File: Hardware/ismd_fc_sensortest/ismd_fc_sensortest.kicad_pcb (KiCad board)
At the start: 2 copper layers, 28 parts, among them U1 TEENSY_4.1

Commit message: sensortest work
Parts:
- removed C19, C20, C21: 100nF, Capacitor_SMD:C_0402_1005Metric
- added C1: 100nF, Capacitor_SMD:C_0201_0603Metric, F.Cu at (42.5, 25.0)
- added C10: 0.1uF, Capacitor_SMD:C_0201_0603Metric, F.Cu at (36.3, 46.0)
- added C2: 100nF, Capacitor_SMD:C_0201_0603Metric, F.Cu at (44.4, 26.1)
- C11: value 0.1uF -> 2.2uF; footprint Capacitor_SMD:C_0402_1005Metric -> Capacitor_SMD:C_0201_0603Metric
- C12: value 2.2uF -> 10nF; footprint Capacitor_SMD:C_0402_1005Metric -> Capacitor_SMD:C_0201_0603Metric
- C13: value 10nF -> 100nF; footprint Capacitor_SMD:C_0402_1005Metric -> Capacitor_SMD:C_0201_0603Metric
- C14, C15, C16, C17, C18, C3, C4, C5, C6, C7, C8, C9: footprint Capacitor_SMD:C_0402_1005Metric -> Capacitor_SMD:C_0201_0603Metric
- I4: value ISM330DLCTR -> ISM330DLC
- moved I2 94.5 mm to (24.5, 26.7)
- moved I3 91.2 mm to (24.7, 35.5)
- moved I4 88.2 mm to (24.6, 44.5)
- moved B4 81.0 mm to (33.5, 26.3), turned to 90 degrees
- moved B5 75.8 mm to (33.6, 35.5)
- moved I1 72.3 mm to (33.7, 44.5)
- moved B1 65.3 mm to (42.4, 26.6)
- moved B2 62.5 mm to (42.5, 35.7)
- moved B3 58.5 mm to (42.8, 44.5)
- moved C5 31.7 mm to (42.9, 46.2)
- moved C6 26.7 mm to (42.5, 42.8), turned to 180 degrees
- moved C11 23.0 mm to (36.3, 45.2), turned to 180 degrees
- moved C12 21.7 mm to (33.5, 46.5)
- moved C16 20.9 mm to (24.5, 37.5)
- moved C8 20.5 mm to (33.4, 33.8), turned to 180 degrees
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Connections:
- C12 pad 1: GND -> +3V3
- C12 pad 2: +3V3 -> GND
- C16 pad 1: GND -> +3V3
- C16 pad 2: +3V3 -> GND
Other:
- board outline added: 102.7 x 40 mm

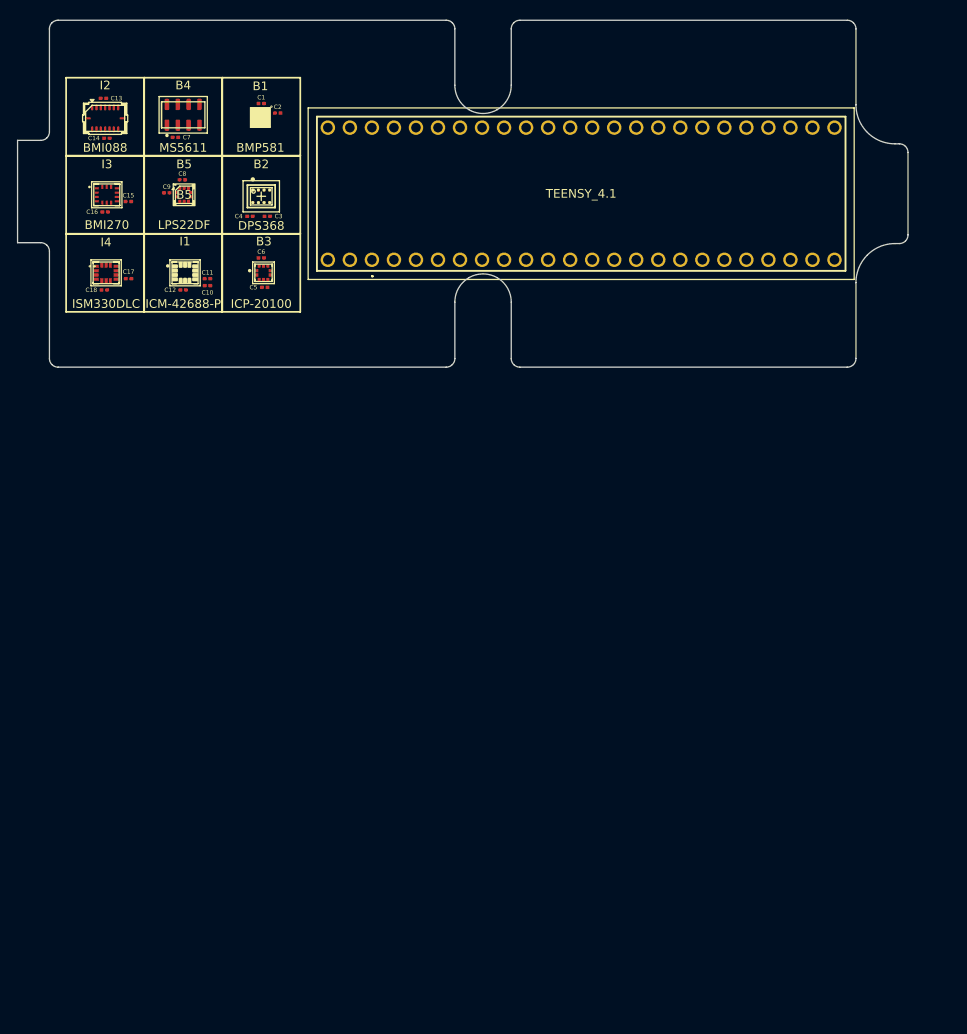
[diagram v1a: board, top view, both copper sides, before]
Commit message: added mounting holes to sensortest
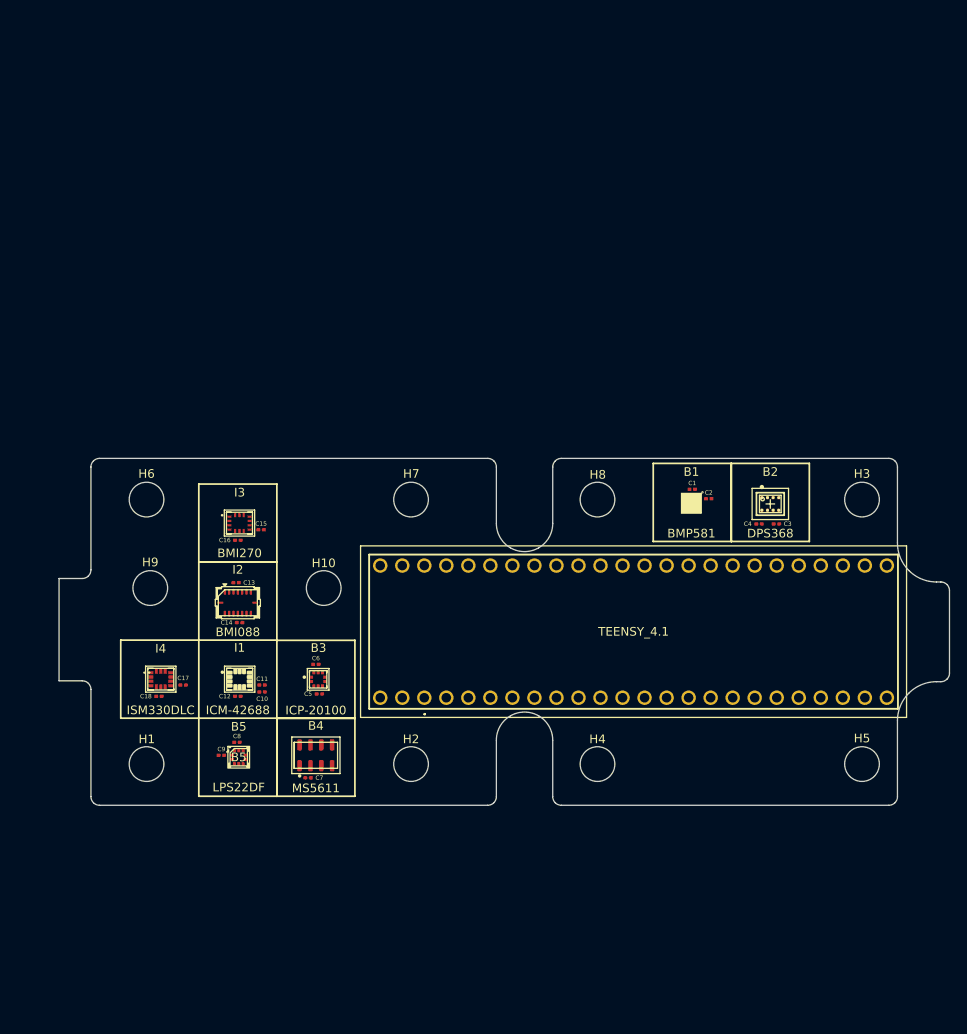
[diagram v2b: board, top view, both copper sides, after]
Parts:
- added H1: MountingHole, MountingHole:MountingHole_4mm, F.Cu at (29.3, 101.2)
- added H10: MountingHole, MountingHole:MountingHole_4mm, F.Cu at (49.7, 80.9)
- added H2: MountingHole, MountingHole:MountingHole_4mm, F.Cu at (59.8, 101.2)
- added H3: MountingHole, MountingHole:MountingHole_4mm, F.Cu at (111.8, 70.7)
- added H4: MountingHole, MountingHole:MountingHole_4mm, F.Cu at (81.3, 101.2)
- added H5: MountingHole, MountingHole:MountingHole_4mm, F.Cu at (111.8, 101.2)
- added H6: MountingHole, MountingHole:MountingHole_4mm, F.Cu at (29.3, 70.7)
- added H7: MountingHole, MountingHole:MountingHole_4mm, F.Cu at (59.8, 70.7)
- added H8: MountingHole, MountingHole:MountingHole_4mm, F.Cu at (81.3, 70.7)
- added H9: MountingHole, MountingHole:MountingHole_4mm, F.Cu at (29.7, 80.9)
- I1: value ICM-42688-P -> ICM-42688
- moved C7 75.4 mm to (47.9, 102.8)
- moved B4 75.4 mm to (48.8, 100.2)
- moved B2 68.6 mm to (101.2, 71.2)
- moved C3 68.6 mm to (101.9, 73.5)
- moved C4 68.6 mm to (99.9, 73.5)
- moved B1 66.7 mm to (92.1, 71.1)
- moved C1 66.7 mm to (92.2, 69.5)
- moved C2 66.7 mm to (94.1, 70.6)
- moved B5 65.2 mm to (39.9, 100.4)
- moved C8 65.2 mm to (39.7, 98.7)
- moved C9 65.2 mm to (37.9, 100.2)
- moved C14 57.9 mm to (40.0, 84.9)
- moved C13 57.9 mm to (39.6, 80.3)
- moved I2 57.9 mm to (39.8, 82.6)
- moved U1 50.9 mm to (61.3, 93.5)
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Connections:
- U1 pad 1: /CS_B6 -> unconnected-(U1-TX1-Pad1)
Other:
- outline, holes or cut-outs redrawn

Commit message: remove mpu holes in sensortest
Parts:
- removed H10, H9: MountingHole, MountingHole:MountingHole_4mm
- U1: value TEENSY_4.1 -> TEENSY 4.1
- moved C17 20.5 mm to (51.5, 82.1)
- moved I4 20.5 mm to (48.9, 81.4)
- moved C18 20.5 mm to (48.7, 83.4)
- moved B3 0.96 mm to (49.0, 90.4)
- moved B5 0.96 mm to (39.9, 99.4)
- moved C5 0.96 mm to (49.2, 92.1)
- moved C8 0.96 mm to (39.7, 97.7)
- moved I1 0.96 mm to (40.0, 90.4)
- moved B4 0.96 mm to (48.8, 99.2)
- moved C10 0.96 mm to (42.6, 91.9)
- moved C11 0.96 mm to (42.6, 91.1)
- moved C12 0.96 mm to (39.8, 92.4)
- moved C13 0.96 mm to (39.6, 79.3)
- moved C14 0.96 mm to (40.0, 83.9)
- moved C15 0.96 mm to (42.5, 73.2)
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
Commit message: power reg
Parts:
- C1, C10, C11, C12, C13, C14, C15, C16, C17, C18, C2, C3, C4, C5, C6, C7, C8, C9: footprint Capacitor_SMD:C_0201_0603Metric -> Capacitor_SMD:C_0402_1005Metric
